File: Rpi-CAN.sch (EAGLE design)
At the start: 22 parts, among them IC1 SN65HVD233-HT, IC2 MCP2510SO, IC3 XC6221B332MR, Q1 20M

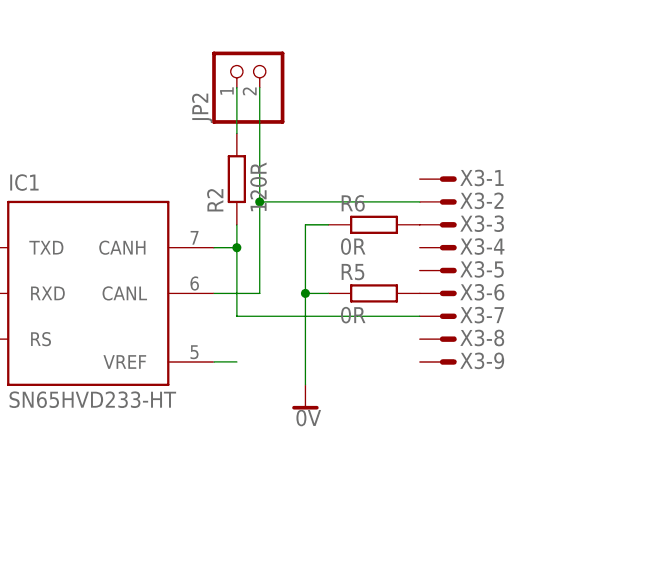
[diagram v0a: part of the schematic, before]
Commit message: Added resitor for connecting Raspberry Pi 5V rail to CAN optional power.
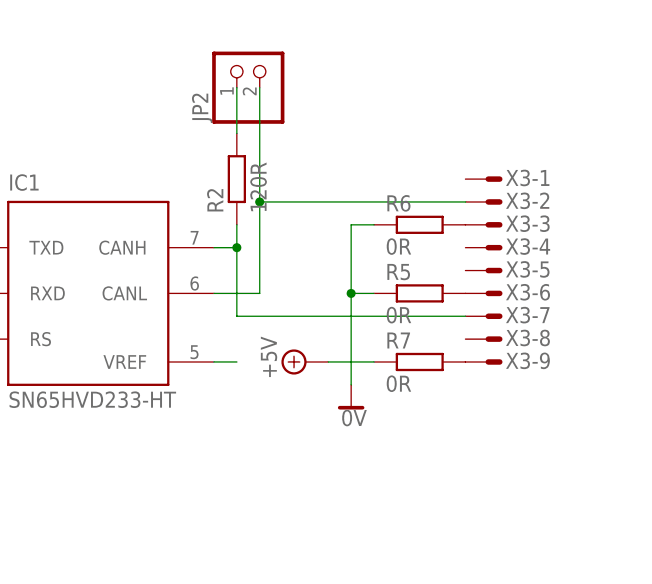
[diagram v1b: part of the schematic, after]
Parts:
- added R7: 0R, rcl:R-EU_R0805
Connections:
- new net N$5: R7.2, X3-9.M
- net +5V: now also R7.1
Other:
- moved on the sheet: R5, R6, X3-1, X3-2, X3-3, X3-4, X3-5, X3-6, X3-7, X3-8, X3-9
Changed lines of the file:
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@@
 <part name="R6" library="rcl" deviceset="R-EU_" device="R0805" value="0R"/>
 <part name="SUPPLY11" library="supply2" deviceset="0V" device=""/>
+<part name="R7" library="rcl" deviceset="R-EU_" device="R0805" value="0R"/>
+<part name="SUPPLY12" library="supply2" deviceset="+5V" device=""/>
 </parts>
 <sheets>
@@
 <instance part="SUPPLY18" gate="0V" x="60.96" y="134.62"/>
 <instance part="SUPPLY1" gate="P" x="132.08" y="215.9"/>
-<instance part="X3" gate="-1" x="139.7" y="101.6"/>
-<instance part="X3" gate="-2" x="139.7" y="99.06"/>
-<instance part="X3" gate="-3" x="139.7" y="96.52"/>
-<instance part="X3" gate="-4" x="139.7" y="93.98"/>
-<instance part="X3" gate="-5" x="139.7" y="91.44"/>
-<instance part="X3" gate="-6" x="139.7" y="88.9"/>
-<instance part="X3" gate="-7" x="139.7" y="86.36"/>
-<instance part="X3" gate="-8" x="139.7" y="83.82"/>
-<instance part="X3" gate="-9" x="139.7" y="81.28"/>
+<instance part="X3" gate="-1" x="144.78" y="101.6"/>
+<instance part="X3" gate="-2" x="144.78" y="99.06"/>
+<instance part="X3" gate="-3" x="144.78" y="96.52"/>
+<instance part="X3" gate="-4" x="144.78" y="93.98"/>
+<instance part="X3" gate="-5" x="144.78" y="91.44"/>
+<instance part="X3" gate="-6" x="144.78" y="88.9"/>
+<instance part="X3" gate="-7" x="144.78" y="86.36"/>
+<instance part="X3" gate="-8" x="144.78" y="83.82"/>
+<instance part="X3" gate="-9" x="144.78" y="81.28"/>
 <instance part="JP1" gate="A" x="81.28" y="187.96"/>
 <instance part="R4" gate="G$1" x="104.14" y="198.12" rot="R90"/>
@@
 <instance part="SUPPLY5" gate="P" x="104.14" y="208.28"/>
 <instance part="SUPPLY7" gate="P" x="71.12" y="208.28"/>
-<instance part="R5" gate="G$1" x="132.08" y="88.9"/>
-<instance part="R6" gate="G$1" x="132.08" y="96.52"/>
-<instance part="SUPPLY11" gate="0V" x="124.46" y="76.2"/>
+<instance part="R5" gate="G$1" x="137.16" y="88.9"/>
+<instance part="R6" gate="G$1" x="137.16" y="96.52"/>
+<instance part="SUPPLY11" gate="0V" x="129.54" y="76.2"/>
+<instance part="R7" gate="G$1" x="137.16" y="81.28"/>
+<instance part="SUPPLY12" gate="+5V" x="124.46" y="81.28" rot="R90"/>
 </instances>
 <busses>
@@
 <pinref part="IC3" gate="G$1" pin="CE"/>
 </segment>
+<segment>
+<pinref part="R7" gate="G$1" pin="1"/>
+<pinref part="SUPPLY12" gate="+5V" pin="+5V"/>
+<wire x1="132.08" y1="81.28" x2="127" y2="81.28" width="0.1524" layer="91"/>
+</segment>
 </net>
 <net name="N$1" class="0">
@@
 <wire x1="114.3" y1="88.9" x2="119.38" y2="88.9" width="0.1524" layer="91"/>
 <wire x1="119.38" y1="88.9" x2="119.38" y2="99.06" width="0.1524" layer="91"/>
-<wire x1="119.38" y1="99.06" x2="137.16" y2="99.06" width="0.1524" layer="91"/>
+<wire x1="119.38" y1="99.06" x2="142.24" y2="99.06" width="0.1524" layer="91"/>
 <wire x1="119.38" y1="111.76" x2="119.38" y2="99.06" width="0.1524" layer="91"/>
 <junction x="119.38" y="99.06"/>
@@
 <net name="N$3" class="0">
 <segment>
-<wire x1="137.16" y1="86.36" x2="116.84" y2="86.36" width="0.1524" layer="91"/>
+<wire x1="142.24" y1="86.36" x2="116.84" y2="86.36" width="0.1524" layer="91"/>
 <wire x1="116.84" y1="86.36" x2="116.84" y2="93.98" width="0.1524" layer="91"/>
 <wire x1="116.84" y1="93.98" x2="114.3" y2="93.98" width="0.1524" layer="91"/>
@@
 <segment>
 <pinref part="R6" gate="G$1" pin="1"/>
-<wire x1="127" y1="96.52" x2="124.46" y2="96.52" width="0.1524" layer="91"/>
-<wire x1="124.46" y1="96.52" x2="124.46" y2="88.9" width="0.1524" layer="91"/>
+<wire x1="132.08" y1="96.52" x2="129.54" y2="96.52" width="0.1524" layer="91"/>
+<wire x1="129.54" y1="96.52" x2="129.54" y2="88.9" width="0.1524" layer="91"/>
 <pinref part="R5" gate="G$1" pin="1"/>
-<wire x1="124.46" y1="88.9" x2="127" y2="88.9" width="0.1524" layer="91"/>
-<wire x1="124.46" y1="88.9" x2="124.46" y2="78.74" width="0.1524" layer="91"/>
+<wire x1="129.54" y1="88.9" x2="132.08" y2="88.9" width="0.1524" layer="91"/>
+<wire x1="129.54" y1="88.9" x2="129.54" y2="78.74" width="0.1524" layer="91"/>
 <pinref part="SUPPLY11" gate="0V" pin="0V"/>
-<junction x="124.46" y="88.9"/>
+<junction x="129.54" y="88.9"/>
 </segment>
 </net>
@@
 </segment>
 </net>
+<net name="N$5" class="0">
+<segment>
+<pinref part="X3" gate="-9" pin="M"/>
+<pinref part="R7" gate="G$1" pin="2"/>
+</segment>
+</net>
